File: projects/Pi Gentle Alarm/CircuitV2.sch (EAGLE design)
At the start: 5 parts, among them X1 RASPI_BOARD_B+_E4, X2 22-23-2021

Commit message: Added template to board
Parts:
- X1: value RASPI_BOARD_B+_E4 -> RASPI_BOARD_B+_E3; device raspberrypi_bastelstube_v13:RASPI_BOARD_B+_E4 -> raspberrypi_bastelstube_v13:RASPI_BOARD_B+_E3
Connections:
- new net N$2: X1.5V0
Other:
- note added: "Checked by:"
- note added: "Drawn by:"
- note added: "FLYFISH TECHNOLOGIES d.o.o."
- note added: "v0.1"
- moved on the sheet: LED1, LED2, Q1, X2-1, X2-2

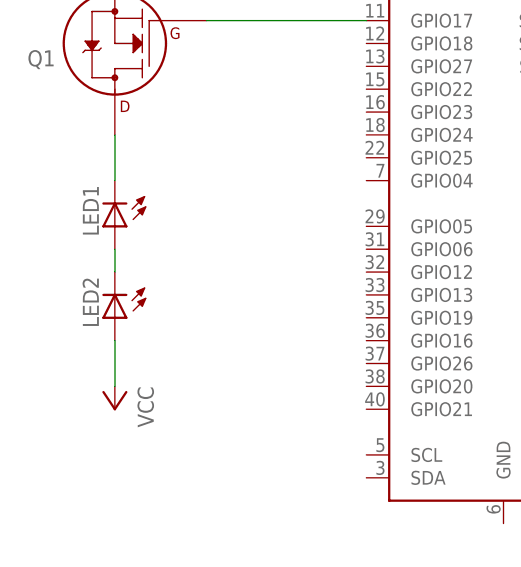
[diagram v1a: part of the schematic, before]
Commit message: Changed two LED to one Large ONe
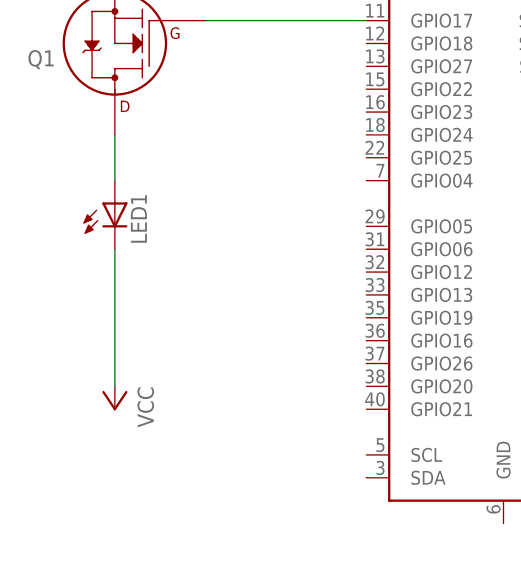
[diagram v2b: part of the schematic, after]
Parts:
- removed LED2: (no value), adafruit:LED3MM
- LED1: device adafruit:LED3MM -> adafruit:LEDSFH482
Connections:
- removed net N$1: LED1.A, LED2.C
- net N$6: now also LED1.A; no longer LED1.C
- net VCC: now also LED1.C; no longer LED2.A
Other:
- moved on the sheet: LED1
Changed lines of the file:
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@@
 <part name="P+1" library="supply1" library_urn="urn:adsk.eagle:library:371" deviceset="VCC" device=""/>
 <part name="GND1" library="supply1" library_urn="urn:adsk.eagle:library:371" deviceset="GND" device=""/>
-<part name="LED1" library="adafruit" library_urn="urn:adsk.eagle:library:420" deviceset="LED" device="3MM" package3d_urn="urn:adsk.eagle:package:6240537/1"/>
-<part name="LED2" library="adafruit" library_urn="urn:adsk.eagle:library:420" deviceset="LED" device="3MM" package3d_urn="urn:adsk.eagle:package:6240537/1"/>
+<part name="LED1" library="adafruit" library_urn="urn:adsk.eagle:library:420" deviceset="LED" device="SFH482" package3d_urn="urn:adsk.eagle:package:6240546/1"/>
 </parts>
 <sheets>
@@
 <attribute name="VALUE" x="48.26" y="185.42" size="1.778" layer="96" rot="R180"/>
 </instance>
-<instance part="LED1" gate="G$1" x="45.72" y="147.32" smashed="yes" rot="R180">
-<attribute name="NAME" x="42.164" y="151.892" size="1.778" layer="95" rot="R270"/>
-<attribute name="VALUE" x="40.005" y="151.892" size="1.778" layer="96" rot="R270"/>
-</instance>
-<instance part="LED2" gate="G$1" x="45.72" y="137.16" smashed="yes" rot="R180">
-<attribute name="NAME" x="42.164" y="141.732" size="1.778" layer="95" rot="R270"/>
-<attribute name="VALUE" x="40.005" y="141.732" size="1.778" layer="96" rot="R270"/>
+<instance part="LED1" gate="G$1" x="45.72" y="149.86" smashed="yes">
+<attribute name="NAME" x="49.276" y="145.288" size="1.778" layer="95" rot="R90"/>
+<attribute name="VALUE" x="51.435" y="145.288" size="1.778" layer="96" rot="R90"/>
 </instance>
 </instances>
@@
 </segment>
 <segment>
-<pinref part="LED2" gate="G$1" pin="A"/>
 <pinref part="P+1" gate="VCC" pin="VCC"/>
-<wire x1="45.72" y1="134.62" x2="45.72" y2="129.54" width="0.1524" layer="91"/>
+<wire x1="45.72" y1="144.78" x2="45.72" y2="129.54" width="0.1524" layer="91"/>
+<pinref part="LED1" gate="G$1" pin="C"/>
 </segment>
 </net>
@@
 <pinref part="Q1" gate="G$1" pin="D"/>
 <wire x1="45.72" y1="152.4" x2="45.72" y2="157.48" width="0.1524" layer="91"/>
-<pinref part="LED1" gate="G$1" pin="C"/>
+<pinref part="LED1" gate="G$1" pin="A"/>
 </segment>
 </net>
-<net name="N$1" class="0">
-<segment>
-<pinref part="LED1" gate="G$1" pin="A"/>
-<pinref part="LED2" gate="G$1" pin="C"/>
-<wire x1="45.72" y1="144.78" x2="45.72" y2="142.24" width="0.1524" layer="91"/>
-</segment>
-</net>

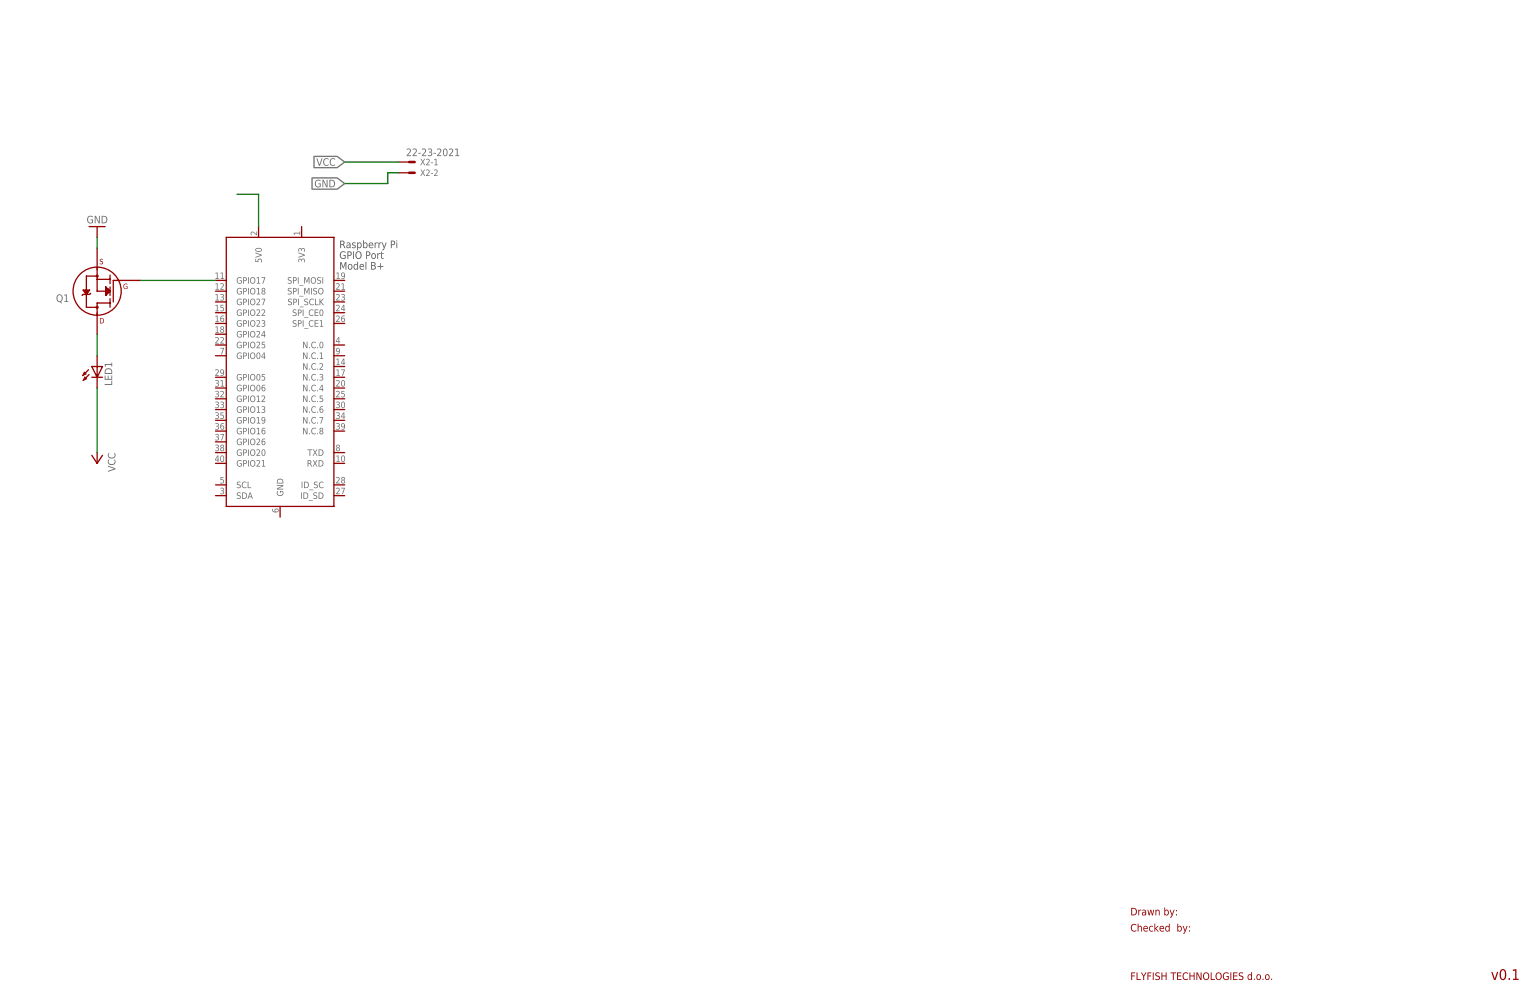
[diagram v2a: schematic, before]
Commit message: Added a fuse to board
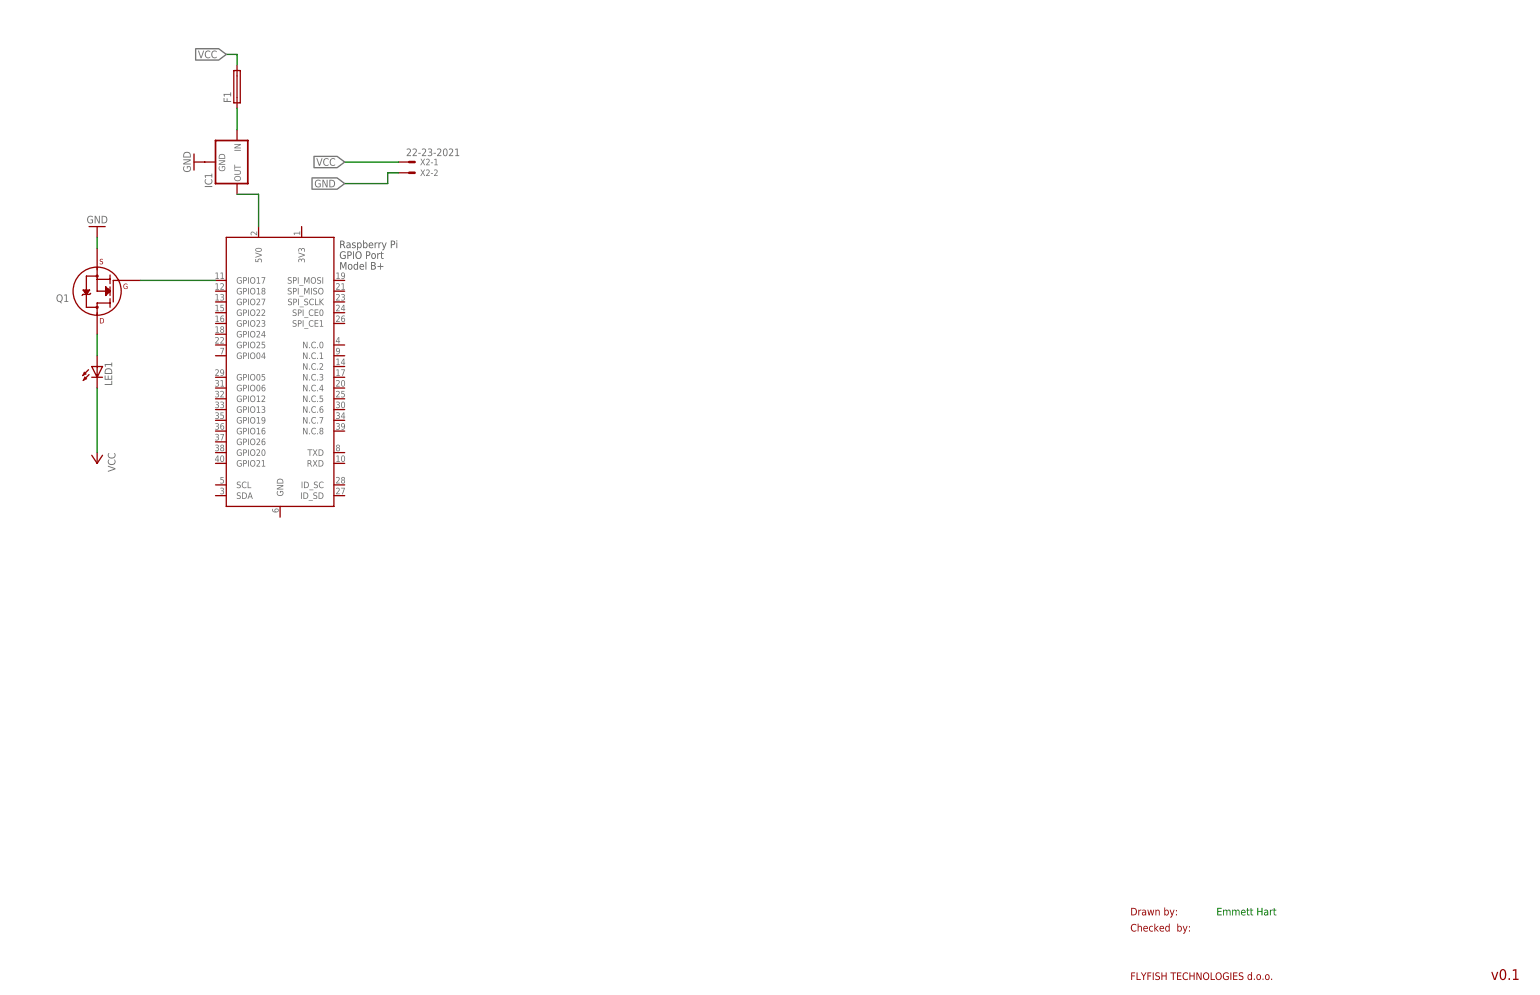
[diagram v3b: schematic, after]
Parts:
- added F1: (no value), fuse:19559
- added IC1: (no value), v-reg:78LXX
- X1: value RASPI_BOARD_B+_E3 -> RASPI_BOARD_B+_E0; device raspberrypi_bastelstube_v13:RASPI_BOARD_B+_E3 -> raspberrypi_bastelstube_v13:RASPI_BOARD_B+_E0
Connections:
- new net N$1: F1.1, IC1.IN
- net GND: now also IC1.GND
- net N$2: now also IC1.OUT
- net VCC: now also F1.2
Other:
- note added: "Emmett Hart"
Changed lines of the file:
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@@
 <parts>
 <part name="FRAME1" library="frames" deviceset="A3L-LOC" device=""/>
-<part name="X1" library="raspberrypi_bastelstube_v13" deviceset="RASPI_BOARD_B+" device="_E3"/>
+<part name="X1" library="raspberrypi_bastelstube_v13" deviceset="RASPI_BOARD_B+" device="_E0" value="RASPI_BOARD_B+_E0"/>
 <part name="X2" library="con-molex" library_urn="urn:adsk.eagle:library:165" deviceset="22-23-2021" device="" package3d_urn="urn:adsk.eagle:package:8078633/1"/>
 <part name="Q1" library="transistors" deviceset="2N700*" device="_TO92" technology="0"/>
@@
 <part name="GND1" library="supply1" library_urn="urn:adsk.eagle:library:371" deviceset="GND" device=""/>
 <part name="LED1" library="adafruit" library_urn="urn:adsk.eagle:library:420" deviceset="LED" device="SFH482" package3d_urn="urn:adsk.eagle:package:6240546/1"/>
+<part name="IC1" library="v-reg" library_urn="urn:adsk.eagle:library:409" deviceset="78LXX" device="" package3d_urn="urn:adsk.eagle:package:30346/1"/>
+<part name="GND2" library="supply1" library_urn="urn:adsk.eagle:library:371" deviceset="GND" device=""/>
+<part name="F1" library="fuse" library_urn="urn:adsk.eagle:library:233" deviceset="19559" device="" package3d_urn="urn:adsk.eagle:package:14056/1"/>
 </parts>
 <sheets>
@@
 <text x="289.56" y="5.08" size="1.778" layer="94">FLYFISH TECHNOLOGIES d.o.o.</text>
 <text x="374.65" y="5.08" size="2.54" layer="94" ratio="10">v0.1</text>
+<text x="309.88" y="20.32" size="1.778" layer="91">Emmett Hart</text>
 </plain>
 <instances>
@@
 <attribute name="VALUE" x="51.435" y="145.288" size="1.778" layer="96" rot="R90"/>
 </instance>
+<instance part="IC1" gate="1" x="78.74" y="198.12" smashed="yes" rot="R270">
+<attribute name="NAME" x="71.12" y="195.58" size="1.778" layer="95" rot="R270"/>
+<attribute name="VALUE" x="68.58" y="195.58" size="1.778" layer="96" rot="R270"/>
+</instance>
+<instance part="GND2" gate="1" x="68.58" y="198.12" smashed="yes" rot="R270">
+<attribute name="VALUE" x="66.04" y="200.66" size="1.778" layer="96" rot="R270"/>
+</instance>
+<instance part="F1" gate="1" x="78.74" y="215.9" smashed="yes" rot="R90">
+<attribute name="NAME" x="77.343" y="212.09" size="1.778" layer="95" rot="R90"/>
+<attribute name="VALUE" x="81.661" y="212.09" size="1.778" layer="96" rot="R90"/>
+</instance>
 </instances>
 <busses>
@@
 <pinref part="LED1" gate="G$1" pin="C"/>
 </segment>
+<segment>
+<pinref part="F1" gate="1" pin="2"/>
+<wire x1="78.74" y1="220.98" x2="78.74" y2="223.52" width="0.1524" layer="91"/>
+<wire x1="78.74" y1="223.52" x2="76.2" y2="223.52" width="0.1524" layer="91"/>
+<label x="76.2" y="223.52" size="1.778" layer="95" rot="R180" xref="yes"/>
+</segment>
 </net>
 <net name="GND" class="0">
@@
 <pinref part="GND1" gate="1" pin="GND"/>
 <wire x1="45.72" y1="177.8" x2="45.72" y2="180.34" width="0.1524" layer="91"/>
+</segment>
+<segment>
+<pinref part="IC1" gate="1" pin="GND"/>
+<pinref part="GND2" gate="1" pin="GND"/>
 </segment>
 </net>
@@
 <wire x1="83.82" y1="190.5" x2="78.74" y2="190.5" width="0.1524" layer="91"/>
 <pinref part="X1" gate="G$1" pin="5V0"/>
+<pinref part="IC1" gate="1" pin="OUT"/>
 </segment>
 </net>
+<net name="N$1" class="0">
+<segment>
+<pinref part="IC1" gate="1" pin="IN"/>
+<wire x1="78.74" y1="205.74" x2="78.74" y2="210.82" width="0.1524" layer="91"/>
+<pinref part="F1" gate="1" pin="1"/>
+</segment>
+</net>

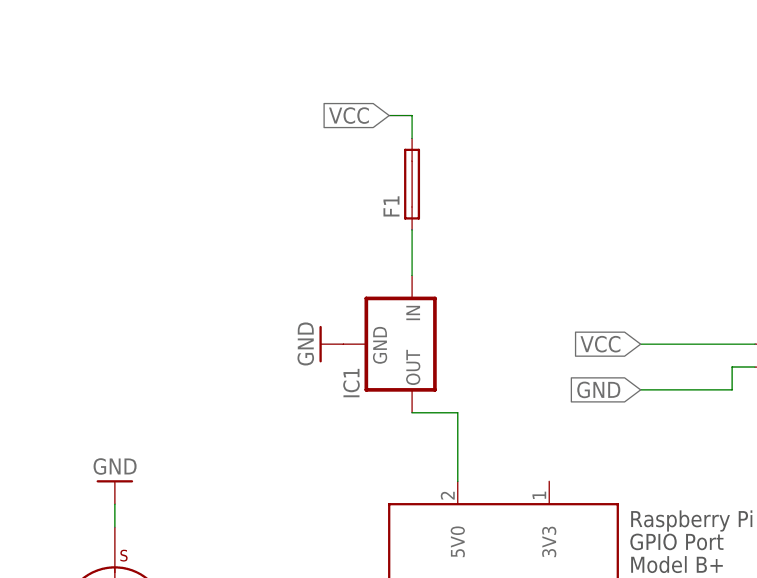
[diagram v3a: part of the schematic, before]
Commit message: Changed fuse to reflect chosen model
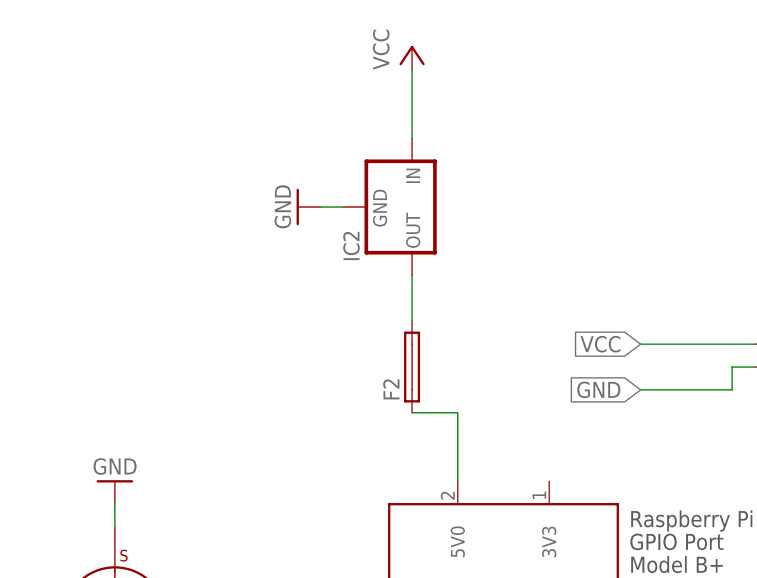
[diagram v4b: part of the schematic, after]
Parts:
- removed F1: (no value), fuse:19559
- removed IC1: (no value), v-reg:78LXX
- added F2: (no value), fuse:TE5
- added IC2: (no value), v-reg:78LXX
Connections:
- net GND: now also IC2.GND; no longer IC1.GND
- net N$1: now also F2.2, IC2.OUT; no longer F1.1, IC1.IN
- net N$2: now also F2.1; no longer IC1.OUT
- net VCC: now also IC2.IN; no longer F1.2
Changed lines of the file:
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@@
 <part name="GND1" library="supply1" library_urn="urn:adsk.eagle:library:371" deviceset="GND" device=""/>
 <part name="LED1" library="adafruit" library_urn="urn:adsk.eagle:library:420" deviceset="LED" device="SFH482" package3d_urn="urn:adsk.eagle:package:6240546/1"/>
-<part name="IC1" library="v-reg" library_urn="urn:adsk.eagle:library:409" deviceset="78LXX" device="" package3d_urn="urn:adsk.eagle:package:30346/1"/>
-<part name="GND2" library="supply1" library_urn="urn:adsk.eagle:library:371" deviceset="GND" device=""/>
-<part name="F1" library="fuse" library_urn="urn:adsk.eagle:library:233" deviceset="19559" device="" package3d_urn="urn:adsk.eagle:package:14056/1"/>
+<part name="P+2" library="supply1" library_urn="urn:adsk.eagle:library:371" deviceset="VCC" device=""/>
+<part name="IC2" library="v-reg" library_urn="urn:adsk.eagle:library:409" deviceset="78LXX" device="" package3d_urn="urn:adsk.eagle:package:30346/1"/>
+<part name="GND3" library="supply1" library_urn="urn:adsk.eagle:library:371" deviceset="GND" device=""/>
+<part name="F2" library="fuse" library_urn="urn:adsk.eagle:library:233" deviceset="TE5" device="" package3d_urn="urn:adsk.eagle:package:14069/1"/>
 </parts>
 <sheets>
@@
 <attribute name="VALUE" x="51.435" y="145.288" size="1.778" layer="96" rot="R90"/>
 </instance>
-<instance part="IC1" gate="1" x="78.74" y="198.12" smashed="yes" rot="R270">
-<attribute name="NAME" x="71.12" y="195.58" size="1.778" layer="95" rot="R270"/>
-<attribute name="VALUE" x="68.58" y="195.58" size="1.778" layer="96" rot="R270"/>
+<instance part="P+2" gate="VCC" x="78.74" y="231.14" smashed="yes">
+<attribute name="VALUE" x="76.2" y="228.6" size="1.778" layer="96" rot="R90"/>
 </instance>
-<instance part="GND2" gate="1" x="68.58" y="198.12" smashed="yes" rot="R270">
-<attribute name="VALUE" x="66.04" y="200.66" size="1.778" layer="96" rot="R270"/>
+<instance part="IC2" gate="1" x="78.74" y="213.36" smashed="yes" rot="R270">
+<attribute name="NAME" x="71.12" y="210.82" size="1.778" layer="95" rot="R270"/>
+<attribute name="VALUE" x="68.58" y="210.82" size="1.778" layer="96" rot="R270"/>
 </instance>
-<instance part="F1" gate="1" x="78.74" y="215.9" smashed="yes" rot="R90">
-<attribute name="NAME" x="77.343" y="212.09" size="1.778" layer="95" rot="R90"/>
-<attribute name="VALUE" x="81.661" y="212.09" size="1.778" layer="96" rot="R90"/>
+<instance part="GND3" gate="1" x="66.04" y="213.36" smashed="yes" rot="R270">
+<attribute name="VALUE" x="63.5" y="215.9" size="1.778" layer="96" rot="R270"/>
+</instance>
+<instance part="F2" gate="1" x="78.74" y="195.58" smashed="yes" rot="R90">
+<attribute name="NAME" x="77.343" y="191.77" size="1.778" layer="95" rot="R90"/>
+<attribute name="VALUE" x="81.661" y="191.77" size="1.778" layer="96" rot="R90"/>
 </instance>
 </instances>
@@
 </segment>
 <segment>
-<pinref part="F1" gate="1" pin="2"/>
-<wire x1="78.74" y1="220.98" x2="78.74" y2="223.52" width="0.1524" layer="91"/>
-<wire x1="78.74" y1="223.52" x2="76.2" y2="223.52" width="0.1524" layer="91"/>
-<label x="76.2" y="223.52" size="1.778" layer="95" rot="R180" xref="yes"/>
+<wire x1="78.74" y1="220.98" x2="78.74" y2="228.6" width="0.1524" layer="91"/>
+<pinref part="P+2" gate="VCC" pin="VCC"/>
+<pinref part="IC2" gate="1" pin="IN"/>
 </segment>
 </net>
@@
 </segment>
 <segment>
-<pinref part="IC1" gate="1" pin="GND"/>
-<pinref part="GND2" gate="1" pin="GND"/>
+<pinref part="IC2" gate="1" pin="GND"/>
+<pinref part="GND3" gate="1" pin="GND"/>
+<wire x1="71.12" y1="213.36" x2="68.58" y2="213.36" width="0.1524" layer="91"/>
 </segment>
 </net>
@@
 <wire x1="83.82" y1="190.5" x2="78.74" y2="190.5" width="0.1524" layer="91"/>
 <pinref part="X1" gate="G$1" pin="5V0"/>
-<pinref part="IC1" gate="1" pin="OUT"/>
+<pinref part="F2" gate="1" pin="1"/>
 </segment>
 </net>
 <net name="N$1" class="0">
 <segment>
-<pinref part="IC1" gate="1" pin="IN"/>
-<wire x1="78.74" y1="205.74" x2="78.74" y2="210.82" width="0.1524" layer="91"/>
-<pinref part="F1" gate="1" pin="1"/>
+<wire x1="78.74" y1="200.66" x2="78.74" y2="205.74" width="0.1524" layer="91"/>
+<pinref part="IC2" gate="1" pin="OUT"/>
+<pinref part="F2" gate="1" pin="2"/>
 </segment>
 </net>
